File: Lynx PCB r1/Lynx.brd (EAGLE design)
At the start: 150 x 50.1 mm, 77 parts, among them IC1 MCP1703DB, Q1 8MHz, X1 BU-SMA-V, X2 332-02, X3 332-02

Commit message: PCB WIP
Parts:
- added C37: 0.1uF, rcl:C0603
- moved 5V_IN 20.8 mm to (142.7, 41.8)
- moved X1 17.3 mm to (118.7, 40.2), turned to 270 degrees
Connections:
- removed net N$14: DAC1.22, R3.1
- removed net N$15: DAC1.21, R4.2
- removed net N$28: DAC2.21, R5.1
- removed net N$29: DAC2.22, R6.2
- new net MOD-RF: IQ_MOD.11, X1.1
- net +3V3: now also C30.1, C31.1, C32.1, C33.1, C37.1
- net BBMI: now also DAC1.21, R4.2
- net BBMQ: now also DAC2.22, R6.2
- net BBPI: now also DAC1.22, R3.1
- net BBPQ: now also DAC2.21, R5.1
- net GND: now also C30.2, C31.2, C32.2, C33.2, C37.2
- net LO: no longer X1.1
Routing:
- net BBMQ: track 0.00 -> 42.2 mm, vias 0 -> 1
- net BBPQ: track 0.00 -> 34.3 mm, vias 0 -> 1
- net GND: track 447.2 -> 476.0 mm
- net BBPI: track 0.00 -> 23.8 mm
- net BBMI: track 0.00 -> 21.1 mm
- net N$14: track 16.6 -> 0.00 mm
- net N$29: track 16.5 -> 0.00 mm
- net N$28: track 13.8 -> 0.00 mm
- net N$15: track 13.8 -> 0.00 mm
- net MOD-RF: track 0.00 -> 8.88 mm
- net +5V: track 19.1 -> 18.9 mm, vias 0 -> 2
- added copper zone on layer 16, net GND
- added copper zone on layer 1, net N$14

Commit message: rf routing
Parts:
- removed STATUS-1, STATUS-2: BI-LED-CC, Lynx components:SOT-23
- added -3V3, BBMI, BBMQ, BBPI, BBPQ, I_BUF, Q_BUF: PTR1PAD1-13Y, testpad:P1-13Y
- added C38, C39, C40: 150pF, rcl:C0603
- added C41, C42: 10uF, rcl:SANYO-OSCON_SMD_B6
- added IC2: (no value), linear:SO08
- added IC3: ICL7660, maxim:SO08
- added R10, R11, R12, R9: 1500, resistor:R0603
- added RESET: DTSM-6, switch-tact:DTSM-6
- added S1, S2: BI-LED-CC, Lynx components:SOT-23
- added U$4, U$5: AD8476, Lynx components:MSOP8
- C37: value 0.1uF -> 150pF
- R3, R6: value 50 -> 100
- R4, R5: value 50 -> 1500
- moved C37 204.7 mm to (92.0, 32.0)
- moved C33 200.9 mm to (112.7, 4.60), turned to 90 degrees
- moved C32 193.8 mm to (108.0, 3.60), turned to 90 degrees
- moved C31 189.2 mm to (104.9, 4.50), turned to 90 degrees
- moved C30 185.1 mm to (102.7, 5.05), turned to 90 degrees
- moved C29 174.7 mm to (85.5, 16.9), turned to 90 degrees
- moved C27 170.2 mm to (74.5, 48.4), turned to 180 degrees
- moved C28 169.2 mm to (85.1, 12.7), turned to 90 degrees
- moved C26 168.6 mm to (77.7, 47.4), turned to 90 degrees
- moved R8 163.9 mm to (85.2, 8.60), turned to 90 degrees
- moved C25 142.9 mm to (76.5, 10.2), turned to 180 degrees
- moved C24 139.8 mm to (76.5, 8.70), turned to 180 degrees
- moved C7 28.9 mm to (93.4, 8.05), turned to 0 degrees
- moved C14 28.4 mm to (121.2, 14.2)
- moved 10MHZ 28.1 mm to (89.8, 12.2), turned to 270 degrees
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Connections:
- removed net MOD-RF: IQ_MOD.11, X1.1
- new net +0.54V: R11.1, R12.2, U$4.3, U$5.3
- new net -3V3: -3V3.TP, C42.-, IC2.4, IC3.5, U$4.7, U$5.7
- new net GND1: IC2.1, IC2.2, I_BUF.TP, R4.1
- new net GND2: IC2.6, IC2.7, Q_BUF.TP, R5.1
- new net N$14: DAC1.22, IC2.3, R3.1
- new net N$29: DAC2.22, IC2.5, R6.2
- new net N$31: C37.2, R4.2, R9.1
- new net N$32: C38.2, R9.2, U$4.8
- new net N$34: C41.-, IC3.4
- new net N$35: C39.2, R10.1, R5.2
- new net N$36: C40.2, R10.2, U$5.8
- new net N$37: C41.+, IC3.2
- net +3V3: now also IC2.8, IC3.8, R11.2, U$4.2, U$5.2; no longer C37.1
- net BBMI: now also BBMI.TP, U$4.5; no longer DAC1.21, R4.2
- net BBMQ: now also BBMQ.TP, U$5.5; no longer DAC2.22, R6.2
- net BBPI: now also BBPI.TP, U$4.4; no longer DAC1.22, R3.1
- net BBPQ: now also BBPQ.TP, U$5.4; no longer DAC2.21, R5.1
- net GND: now also C37.1, C38.1, C39.1, C40.1, C42.+, DAC1.21, DAC2.21, IC3.3, IC3.6, R12.1, RESET.3, RESET.4, S1.3, S2.3, U$4.1, U$5.1; no longer C37.2, R4.1, R5.2, STATUS-1.3, STATUS-2.3
- net LO: now also X1.1
- net N$16: now also S1.1; no longer STATUS-1.1
- net N$17: now also S1.2; no longer STATUS-1.2
- net N$18: now also S2.1; no longer STATUS-2.1
- net N$19: now also S2.2; no longer STATUS-2.2
- net NRST: now also RESET.1, RESET.2
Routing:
- net +3V3: track 320.1 -> 383.9 mm, vias 11 -> 18
- net SPI2-MISO: track 141.9 -> 91.0 mm
- net SPI2-MOSI: track 139.0 -> 89.2 mm
- net SPI2-SCK: track 138.0 -> 89.3 mm
- net SPI2-CS: track 137.9 -> 90.4 mm
- net -3V3: track 0.00 -> 43.9 mm, vias 0 -> 3
- net N$14: track 0.00 -> 28.2 mm
- net BBMQ: track 42.2 -> 63.8 mm, vias 1 -> 2
- net N$29: track 0.00 -> 21.3 mm
- net BBPQ: track 34.3 -> 53.1 mm, vias 1 -> 0
- net BBMI: track 21.1 -> 38.8 mm, vias 0 -> 2
- net LO: track 2.00 -> 17.4 mm
- net NRST: track 21.1 -> 35.4 mm, vias 2 -> 3
- net GND: track 476.0 -> 490.2 mm, vias 12 -> 14
- net GND2: track 0.00 -> 11.3 mm
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- removed copper zone on layer 16, net GND
- removed copper zone on layer 1, net N$14
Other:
- board size 150 x 50.1 mm -> 150.1 x 51 mm
- board text removed: "Low pass magic"

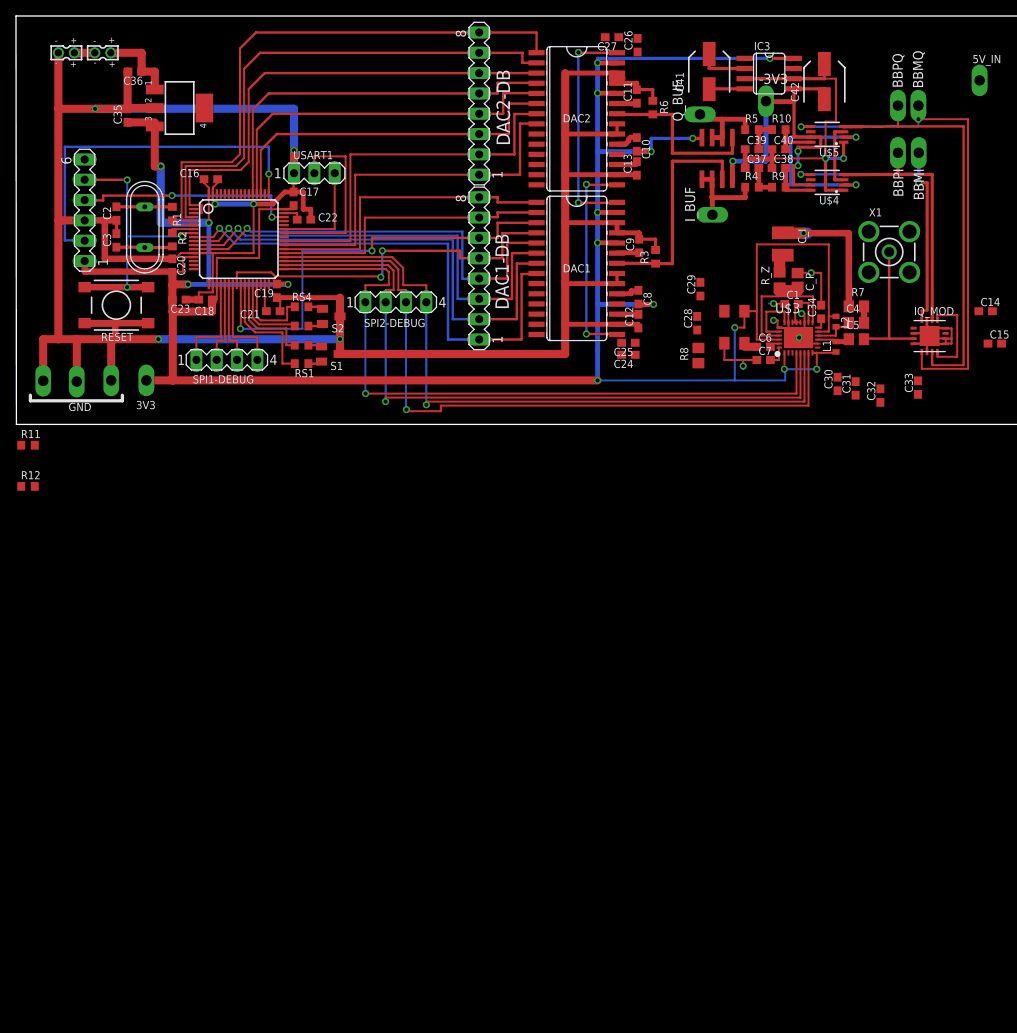
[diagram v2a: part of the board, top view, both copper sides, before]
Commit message: Power supply and jumpers
So many jumpers
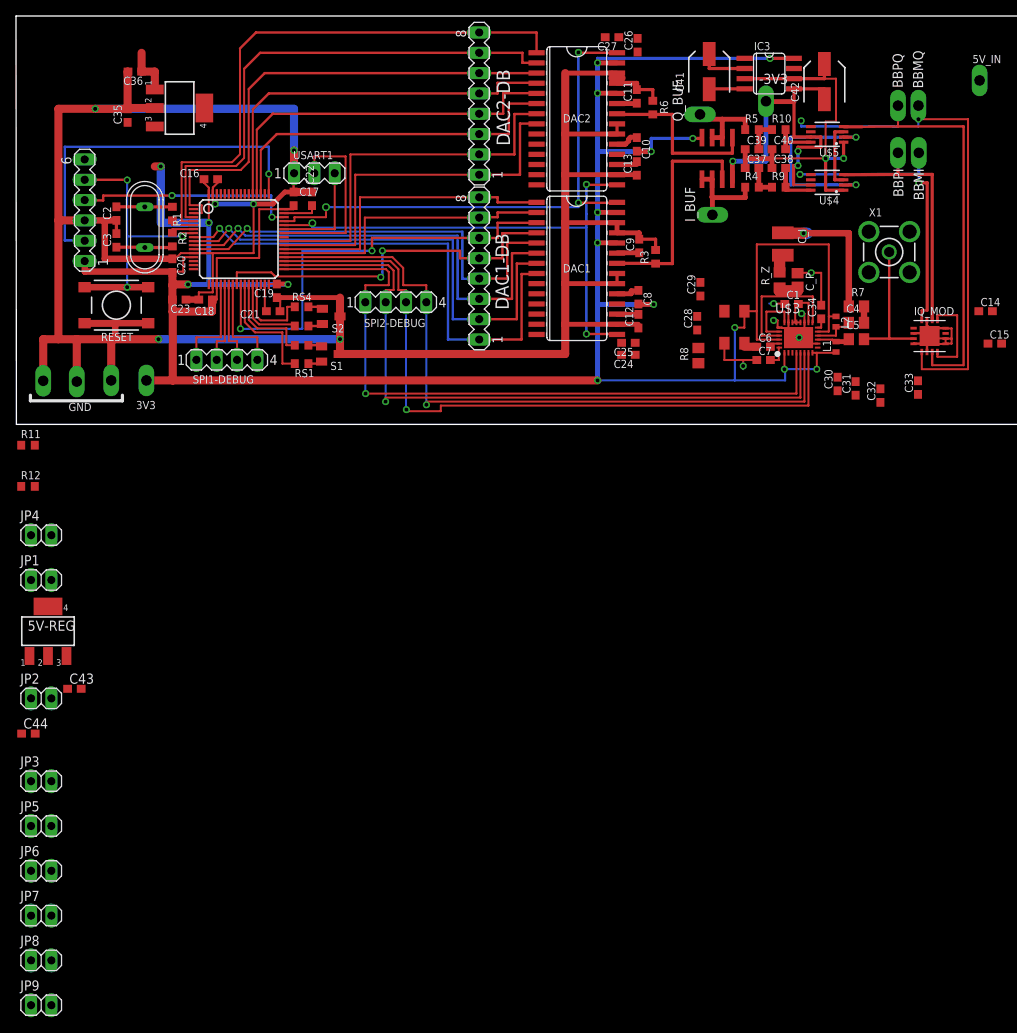
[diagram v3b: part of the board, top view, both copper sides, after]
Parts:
- removed X2, X3: 332-02, con-garry:332-02
- added 5V-REG: MCP1703DB, linear:SOT223
- added C43, C44: 0.1uF, rcl:C0603
- added JP1, JP2, JP3, JP4, JP5, JP6, JP7, JP8, JP9: (no value), pinhead:1X02
- moved C22 2.79 mm to (37.0, 28.2), turned to 90 degrees
- renumbered IC1 to 3V3-REG, U$2 to SWD-HEADER
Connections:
- removed net BATTERY-OUT: 3V3-REG.1, C36.1, X2.1
- removed net DAC_SLEEP: DAC1.15, DAC2.15
- removed net N$43: X2.2, X3.1
- new net DAC-SLEEP: DAC1.15, DAC2.15, U$1.44
- new net N$15: JP6.2, U$5.5
- new net N$28: JP7.1, U$5.4
- new net N$38: 3V3-REG.3, C35.1, JP1.1
- new net N$39: 5V-REG.3, C43.1, JP2.1
- new net N$40: JP8.2, U$4.4
- new net N$41: JP9.1, U$4.5
- new net POWER-IN: 3V3-REG.1, 5V-REG.1, C36.1, C44.1, JP5.2
- net +3V3: now also JP1.2, JP3.2; no longer 3V3-REG.3, C35.1
- net +5V: now also JP2.2, JP4.2
- net BBMI: now also JP8.1; no longer U$4.5
- net BBMQ: now also JP6.1; no longer U$5.5
- net BBPI: now also JP9.2; no longer U$4.4
- net BBPQ: now also JP7.2; no longer U$5.4
- net DAC-CLK: now also U$1.45
- net GND: now also 5V-REG.2, C43.2, C44.2, JP3.1, JP4.1, JP5.1; no longer X3.2
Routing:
- net DAC-SLEEP: track 0.00 -> 66.8 mm, vias 0 -> 3
- net DAC-CLK: track 28.6 -> 67.6 mm, vias 2 -> 3
- net DAC_SLEEP: track 26.5 -> 0.00 mm, vias 2 -> 0
- net GND: track 490.2 -> 479.9 mm
- net BATTERY-OUT: track 10.1 -> 0.00 mm
- net +3V3: track 383.9 -> 375.0 mm
- net POWER-IN: track 0.00 -> 6.24 mm
- net N$43: track 2.55 -> 0.00 mm
- net N$27: track 2.46 -> 4.44 mm
- net BBMI: track 38.8 -> 37.6 mm
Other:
- board text removed: "+"
- board text removed: "-"

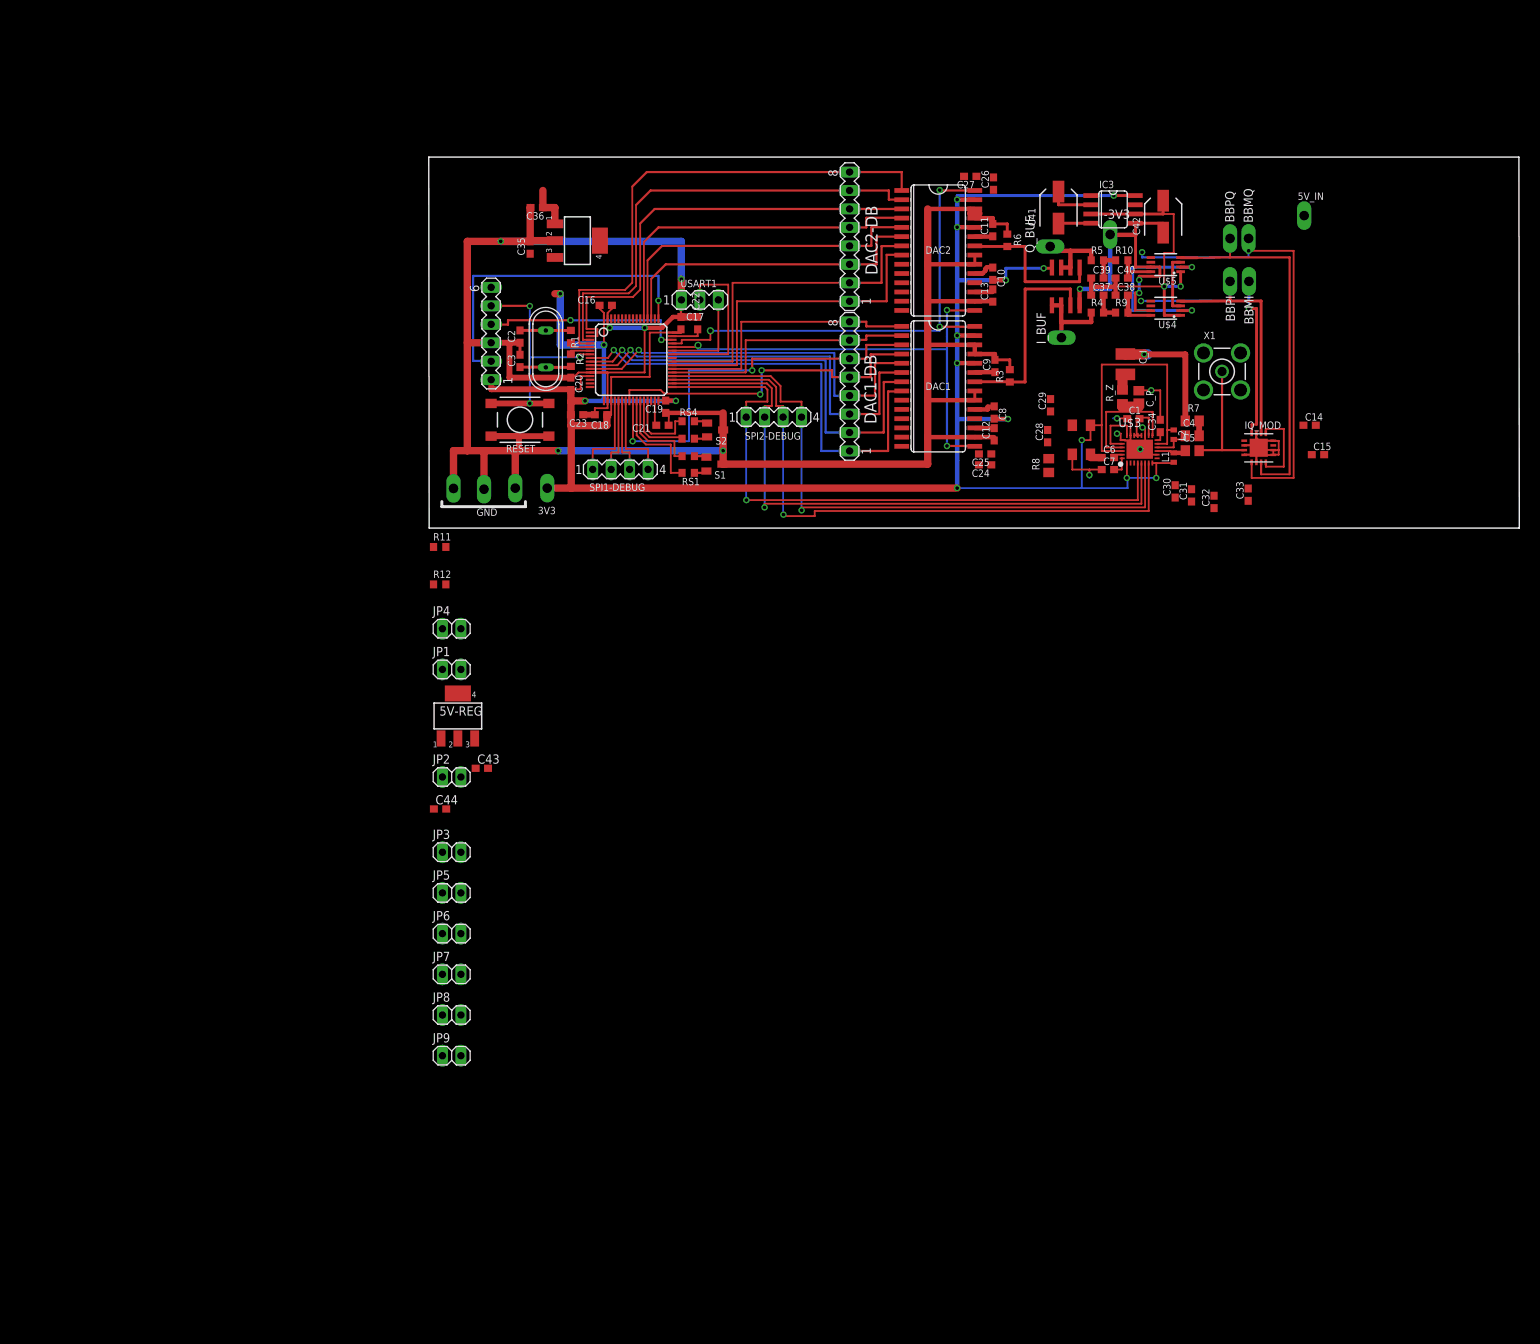
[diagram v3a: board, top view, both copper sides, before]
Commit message: Complete rf reroute
Shuffled a 'lot' of things around. Ripped up everything past the op-amps
and made it a lot nicer.
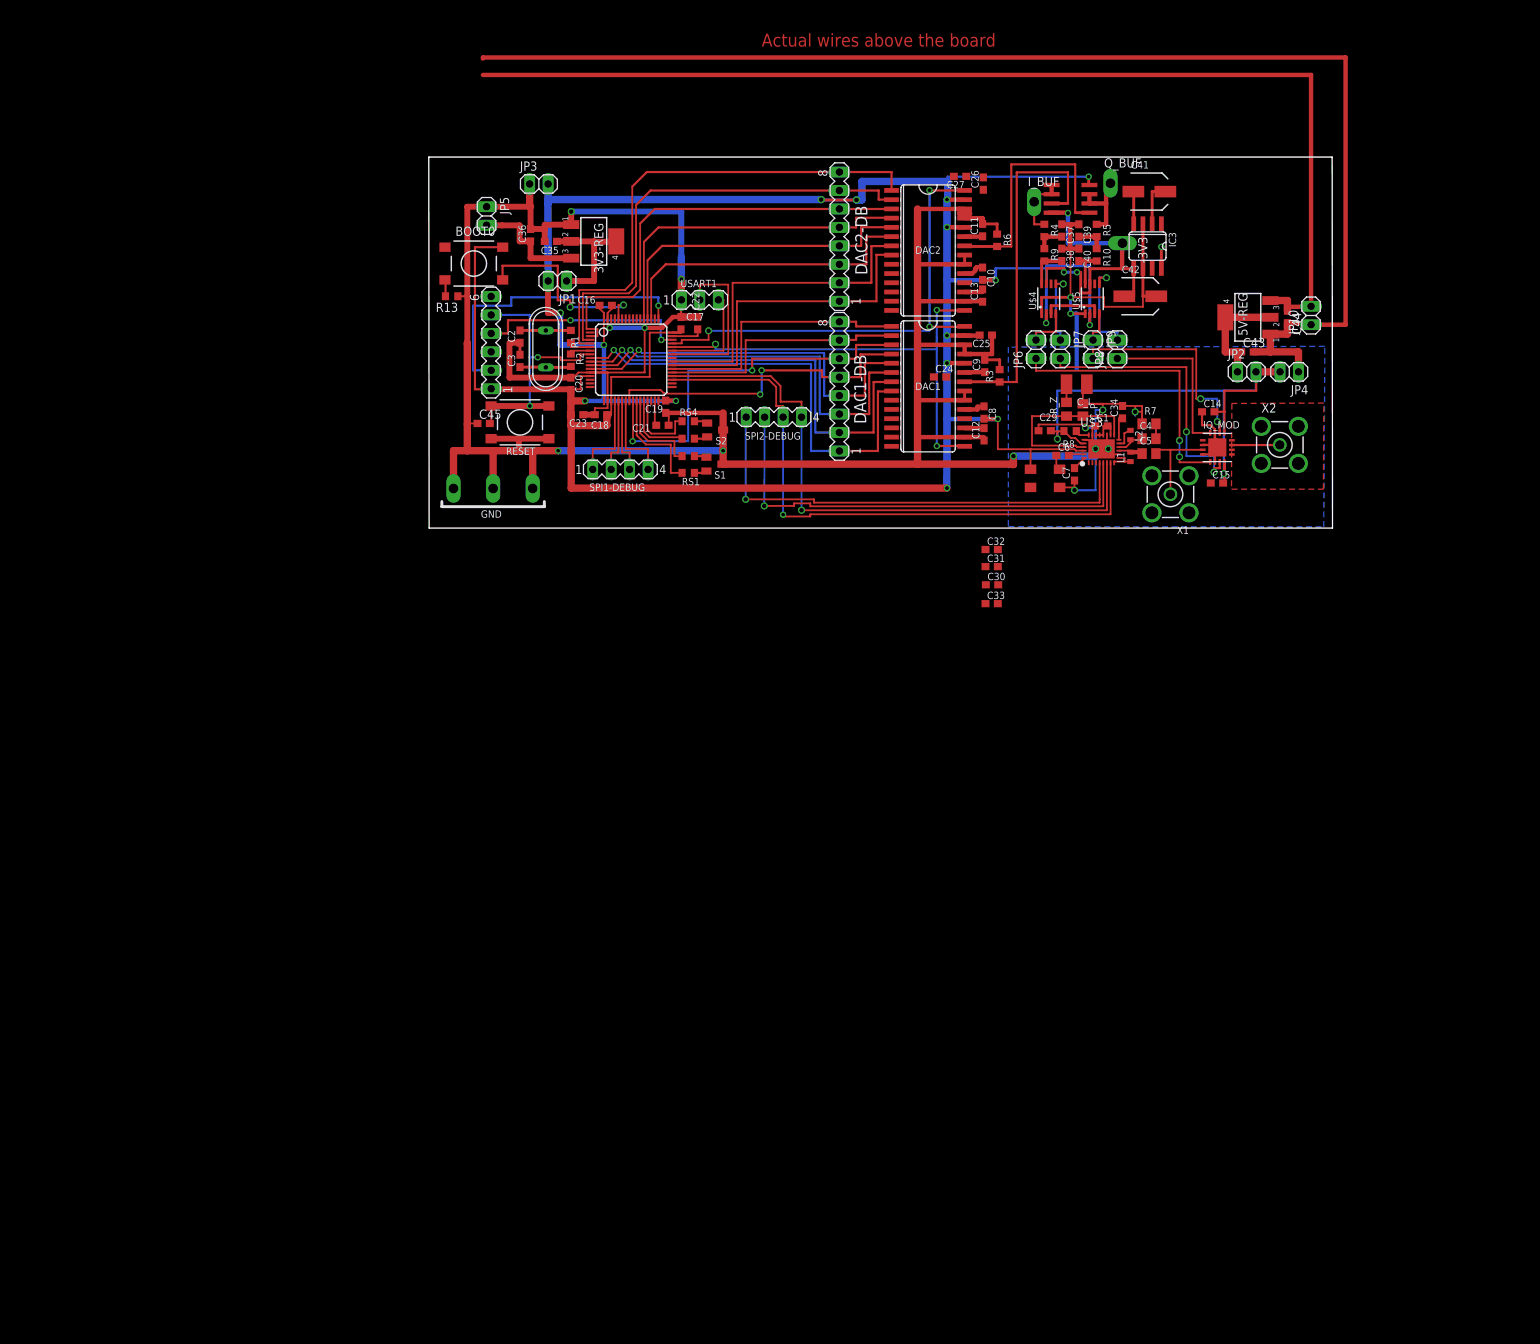
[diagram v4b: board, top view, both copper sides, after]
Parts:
- removed 3V3, 5V_IN, BBMI, BBMQ, BBPI, BBPQ: PTR1PAD1-13Y, testpad:P1-13Y
- removed C28: 1uF, rcl:C0603
- removed R11, R12: 1500, resistor:R0603
- added BOOT0: DTSM-6, switch-tact:DTSM-6
- added C45: 0.1uF, rcl:C0603
- added JP10: Power In, pinhead:1X02
- added R13: 1500, resistor:R0603
- added X2: BU-SMA-V, con-coax:BU-SMA-V
- 3V3-REG, 5V-REG: value MCP1703DB -> V-REG; device linear:SOT223 -> Lynx components:SOT223
- C35, C36, C43, C44: value 0.1uF -> 1uF
- JP1: value (none) -> 3v3 reg
- JP2: value (none) -> 5v reg
- JP3: value (none) -> 3v3 in
- JP4: value (none) -> 5v in
- JP5: value (none) -> Power In
- JP6: value (none) -> BBMQ
- JP7: value (none) -> BBPQ
- JP8: value (none) -> BBMI
- JP9: value (none) -> BBPI
- R8: device rcl:R0805 -> rcl:R0603
- moved C44 134.8 mm to (118.1, 29.1), turned to 270 degrees
- moved JP9 131.3 mm to (91.3, 24.6), turned to 270 degrees
- moved JP8 129.5 mm to (94.7, 24.6), turned to 90 degrees
- moved JP2 122.8 mm to (112.5, 21.5)
- moved 5V-REG 121.8 mm to (112.7, 29.0), turned to 90 degrees
- moved JP4 120.5 mm to (118.3, 21.5), turned to 180 degrees
- moved JP7 120.0 mm to (86.8, 24.6), turned to 270 degrees
- moved C43 119.9 mm to (112.6, 24.2)
- moved JP6 113.7 mm to (83.5, 24.6), turned to 90 degrees
- moved JP5 93.3 mm to (7.90, 43.0), turned to 270 degrees
- moved JP3 92.7 mm to (15.1, 47.4)
- moved JP1 55.4 mm to (17.6, 34.0), turned to 180 degrees
- moved C33 38.4 mm to (77.4, -10.4), turned to 0 degrees
- moved C32 31.3 mm to (77.4, -2.95), turned to 0 degrees
- moved C31 29.2 mm to (77.4, -5.30), turned to 0 degrees
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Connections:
- net GND1 renamed I_BUF
- net GND2 renamed Q_BUF
- removed net N$41: JP9.1, U$4.5
- removed net PLL_MUTE: U$3.9
- new net 5V-REG: 5V-REG.2, 5V-REG.4, C43.1, JP2.1
- new net N$30: R8.1, U$3.22
- new net RF-MOD: IQ_MOD.11, X2.1
- net +0.54V: no longer R11.1, R12.2
- net +3V3: now also BOOT0.1, BOOT0.2, U$3.9; no longer 3V3.TP, R11.2
- net +5V: no longer 5V_IN.TP, C28.2, R8.1, U$3.22
- net BBMI: no longer BBMI.TP
- net BBMQ: no longer BBMQ.TP
- net BBPI: no longer BBPI.TP
- net BBPQ: no longer BBPQ.TP
- net BOOT0: now also BOOT0.3, BOOT0.4, R13.2
- net GND: now also 3V3-REG.1, 5V-REG.1, C45.1, JP10.1, R13.1, X2.2, X2.3, X2.4, X2.5; no longer 3V3-REG.2, 5V-REG.2, C28.1, R12.1
- net N$15: now also U$4.4; no longer U$5.5
- net N$28: now also U$4.5; no longer U$5.4
- net N$38: now also 3V3-REG.2, 3V3-REG.4; no longer 3V3-REG.3
- net N$39: now also JP8.2, U$5.5; no longer 5V-REG.3, C43.1, JP2.1
- net N$40: now also JP9.1, U$5.4; no longer JP8.2, U$4.4
- net NRST: now also C45.2
- net POWER-IN: now also 3V3-REG.3, 5V-REG.3, JP10.2; no longer 3V3-REG.1, 5V-REG.1
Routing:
- net GND: track 479.9 -> 706.1 mm, vias 14 -> 15
- net POWER-IN: track 6.24 -> 169.1 mm
- net +5V: track 19.1 -> 76.6 mm, vias 0 -> 2
- net +3V3: track 375.0 -> 420.9 mm, vias 18 -> 17
- net BOOT0: track 0.00 -> 29.5 mm, vias 0 -> 2
- net BBMQ: track 63.5 -> 38.3 mm
- net SPI2-CS: track 90.4 -> 66.0 mm
- net SPI2-SCK: track 89.3 -> 65.6 mm
- net N$14: track 28.2 -> 49.6 mm
- net N$38: track 0.00 -> 17.4 mm
- net 5V-REG: track 0.00 -> 15.9 mm
- net BBMI: track 37.6 -> 23.0 mm, vias 2 -> 0
- net N$39: track 0.00 -> 13.9 mm, vias 0 -> 1
- net N$29: track 21.3 -> 35.2 mm
- net BBPQ: track 53.0 -> 39.5 mm, vias 0 -> 2
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- added copper zone on layer 1, net GND
- added copper zone on layer 16, net GND
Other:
- board size 150.1 x 51 mm -> 124.3 x 51 mm
- board text added: "Actual wires above the board"
